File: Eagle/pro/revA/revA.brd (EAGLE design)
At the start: 100 x 88 mm, 57 parts, among them Q1 20MHz, U1 MCP42XXX

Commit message: silkscreen
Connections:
- net N$22 renamed LCD_GND
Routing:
- net N$28: track 106.1 -> 141.6 mm
- net N$21: track 132.2 -> 129.7 mm
- net N$29: track 94.9 -> 94.3 mm
- added copper zone on layer 1, net GND
- added copper zone on layer 16, net GND
- added copper zone on layer 1, net LCD_GND
- added copper zone on layer 16, net LCD_GND
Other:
- board size 100 x 88 mm -> 100 x 90 mm
- board text added: "Analyser"
- board text added: "Ashley J. Robinson"
- board text added: "Audio"
- board text added: "AudioSpectrumAnalyser"
- board text added: "DBG_UART"
- board text added: "GND"
- board text added: "IN"
- board text added: "OUT"
- board text added: "RESET"
- board text added: "RevA May 2014"
- board text added: "SW1"
- board text added: "SW2"
- board text added: "Spectrum"
- board text added: "TRIM"
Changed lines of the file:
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@@
 <setting verticaltext="up"/>
 </settings>
-<grid distance="0.5" unitdist="mm" unit="mm" style="lines" multiple="1" display="yes" altdistance="0.1" altunitdist="mm" altunit="mm"/>
+<grid distance="1" unitdist="mm" unit="mm" style="lines" multiple="1" display="yes" altdistance="0.1" altunitdist="mm" altunit="mm"/>
 <layers>
 <layer number="1" name="Top" color="4" fill="1" visible="yes" active="yes"/>
@@
 <board>
 <plain>
-<wire x1="0" y1="6" x2="0" y2="54" width="0" layer="20"/>
-<wire x1="6" y1="0" x2="94" y2="0" width="0" layer="20"/>
-<wire x1="100" y1="54" x2="100" y2="6" width="0" layer="20"/>
-<wire x1="6" y1="0" x2="0" y2="6" width="0" layer="20" curve="-90"/>
-<wire x1="100" y1="6" x2="94" y2="0" width="0" layer="20" curve="-90"/>
-<wire x1="0" y1="54" x2="6" y2="60" width="0" layer="20" curve="-90"/>
-<wire x1="8" y1="66" x2="8" y2="82" width="0" layer="20"/>
-<wire x1="14" y1="88" x2="87" y2="88" width="0" layer="20"/>
-<wire x1="92" y1="82" x2="92" y2="66" width="0" layer="20"/>
-<wire x1="92" y1="66" x2="86" y2="60" width="0" layer="20" curve="-90"/>
-<wire x1="87" y1="88" x2="92" y2="82" width="0" layer="20" curve="-90"/>
-<wire x1="8" y1="82" x2="14" y2="88" width="0" layer="20" curve="-90"/>
-<hole x="14.4" y="60" drill="0.5"/>
 <hole x="15.2" y="60" drill="0.5"/>
-<hole x="13.6" y="60" drill="0.5"/>
 <hole x="16.8" y="60" drill="0.5"/>
 <hole x="17.6" y="60" drill="0.5"/>
@@
 <hole x="84" y="60" drill="0.5"/>
 <hole x="82.4" y="60" drill="0.5"/>
+<hole x="84.8" y="60" drill="0.5"/>
+<hole x="12" y="60" drill="0.5"/>
+<hole x="13.6" y="60" drill="0.5"/>
+<hole x="14.4" y="60" drill="0.5"/>
+<hole x="12.8" y="60" drill="0.5"/>
+<hole x="4.8" y="60" drill="0.5"/>
+<hole x="6.4" y="60" drill="0.5"/>
+<hole x="7.2" y="60" drill="0.5"/>
+<hole x="5.6" y="60" drill="0.5"/>
+<hole x="8.8" y="60" drill="0.5"/>
+<hole x="9.6" y="60" drill="0.5"/>
+<hole x="8" y="60" drill="0.5"/>
+<hole x="11.2" y="60" drill="0.5"/>
+<hole x="10.4" y="60" drill="0.5"/>
+<hole x="1.6" y="60" drill="0.5"/>
+<hole x="3.2" y="60" drill="0.5"/>
+<hole x="4" y="60" drill="0.5"/>
+<hole x="2.4" y="60" drill="0.5"/>
+<hole x="0.8" y="60" drill="0.5"/>
 <hole x="85.6" y="60" drill="0.5"/>
 <hole x="86.4" y="60" drill="0.5"/>
-<hole x="84.8" y="60" drill="0.5"/>
-<wire x1="14" y1="60" x2="8" y2="66" width="0" layer="20" curve="-90"/>
-<wire x1="6" y1="60" x2="14" y2="60" width="0" layer="20"/>
-<wire x1="94" y1="60" x2="100" y2="54" width="0" layer="20" curve="-90"/>
-<wire x1="86" y1="60" x2="94" y2="60" width="0" layer="20"/>
+<hole x="88" y="60" drill="0.5"/>
+<hole x="88.8" y="60" drill="0.5"/>
+<hole x="87.2" y="60" drill="0.5"/>
+<hole x="90.4" y="60" drill="0.5"/>
+<hole x="91.2" y="60" drill="0.5"/>
+<hole x="89.6" y="60" drill="0.5"/>
+<hole x="92.8" y="60" drill="0.5"/>
+<hole x="93.6" y="60" drill="0.5"/>
+<hole x="92" y="60" drill="0.5"/>
+<hole x="95.2" y="60" drill="0.5"/>
+<hole x="96" y="60" drill="0.5"/>
+<hole x="94.4" y="60" drill="0.5"/>
+<hole x="97.6" y="60" drill="0.5"/>
+<hole x="98.4" y="60" drill="0.5"/>
+<hole x="96.8" y="60" drill="0.5"/>
+<hole x="99.2" y="60" drill="0.5"/>
+<wire x1="0" y1="6" x2="0" y2="84" width="0" layer="20"/>
+<wire x1="6" y1="90" x2="94" y2="90" width="0" layer="20"/>
+<wire x1="100" y1="84" x2="100" y2="6" width="0" layer="20"/>
+<wire x1="94" y1="0" x2="6" y2="0" width="0" layer="20"/>
+<wire x1="6" y1="0" x2="0" y2="6" width="0" layer="20" curve="-90"/>
+<wire x1="100" y1="6" x2="94" y2="0" width="0" layer="20" curve="-90"/>
+<wire x1="0" y1="84" x2="6" y2="90" width="0" layer="20" curve="-90"/>
+<wire x1="94" y1="90" x2="100" y2="84" width="0" layer="20" curve="-90"/>
+<text x="3" y="28" size="1.778" layer="21" font="vector">OUT</text>
+<text x="93" y="28" size="1.778" layer="21" font="vector">IN</text>
+<text x="3" y="11" size="1.778" layer="21" font="vector">OUT</text>
+<text x="93" y="11" size="1.778" layer="21" font="vector">IN</text>
+<text x="76" y="1" size="1.778" layer="21" font="vector">RESET</text>
+<text x="57" y="1" size="1.778" layer="21" font="vector">TRIM</text>
+<text x="38" y="1" size="1.778" layer="21" font="vector">SW2</text>
+<text x="18" y="1" size="1.778" layer="21" font="vector">SW1</text>
+<text x="27" y="52" size="1.778" layer="21" font="vector" rot="R270">GND</text>
+<text x="21" y="52" size="1.778" layer="21" font="vector" rot="R270">OUT</text>
+<text x="24" y="52" size="1.778" layer="21" font="vector" rot="R270">IN</text>
+<text x="20" y="43" size="1.778" layer="21" font="vector" rot="R90">DBG_UART</text>
+<text x="96" y="45" size="1.778" layer="22" font="vector" rot="MR0">Ashley J. Robinson</text>
+<text x="96" y="48" size="1.778" layer="22" font="vector" rot="MR0">AudioSpectrumAnalyser</text>
+<text x="96" y="42" size="1.778" layer="22" font="vector" rot="MR0">RevA May 2014</text>
+<text x="3" y="86" size="1.778" layer="21" font="vector">Audio</text>
+<text x="6" y="83" size="1.778" layer="21" font="vector">Spectrum</text>
+<text x="9" y="80" size="1.778" layer="21" font="vector">Analyser</text>
+<text x="1" y="76" size="1.778" layer="21" font="vector">Ashley J. Robinson</text>
+<text x="1" y="73" size="1.778" layer="21" font="vector">RevA May 2014</text>
 </plain>
 <attributes>
@@
 <wire x1="49.2508875" y1="38.2508875" x2="49.74709375" y2="38.74709375" width="0.254" layer="1"/>
 <wire x1="49.74709375" y1="38.74709375" x2="49.74709375" y2="42.0008875" width="0.254" layer="1"/>
+<polygon width="0.254" layer="16">
+<vertex x="-1" y="-1"/>
+<vertex x="-1" y="59"/>
+<vertex x="101" y="59"/>
+<vertex x="101" y="-1"/>
+</polygon>
+<polygon width="0.4064" layer="1">
+<vertex x="-1" y="-1"/>
+<vertex x="-1" y="59"/>
+<vertex x="101" y="59"/>
+<vertex x="101" y="-1"/>
+</polygon>
 </signal>
 <signal name="N$1">
@@
 <contactref element="SV2" pad="10"/>
 <contactref element="SV1" pad="1"/>
-<wire x1="9" y1="68.5" x2="26.5" y2="86" width="0.6096" layer="1"/>
-<wire x1="26.5" y1="86" x2="37.5" y2="86" width="0.6096" layer="1"/>
 <wire x1="37.5" y1="86" x2="37.5" y2="84" width="0.6096" layer="1"/>
 <wire x1="37.5" y1="84" x2="41.5" y2="80" width="0.6096" layer="1"/>
 <wire x1="41.5" y1="80" x2="72.5" y2="80" width="0.6096" layer="1"/>
-<wire x1="72.5" y1="80" x2="83.3" y2="69.2" width="0.6096" layer="1"/>
+<wire x1="72.5" y1="80" x2="79.5" y2="73" width="0.6096" layer="1"/>
+<wire x1="81.75" y1="70.75" x2="83.3" y2="69.2" width="0.6096" layer="1"/>
 <wire x1="83.3" y1="69.2" x2="83.3" y2="65.5" width="0.6096" layer="1"/>
 <wire x1="83.3" y1="65.5" x2="83.8" y2="65" width="0.6096" layer="1"/>
 <wire x1="83.8" y1="65" x2="85.81" y2="65" width="0.6096" layer="1"/>
 <wire x1="85.81" y1="65" x2="87.08" y2="66.27" width="0.6096" layer="1"/>
-<wire x1="12.92" y1="63.73" x2="9.77" y2="63.73" width="0.6096" layer="1"/>
-<wire x1="9.77" y1="63.73" x2="9" y2="64.5" width="0.6096" layer="1"/>
-<wire x1="9" y1="64.5" x2="9" y2="68.5" width="0.6096" layer="1"/>
+<wire x1="12.92" y1="63.73" x2="11.27" y2="63.73" width="0.6096" layer="1"/>
+<wire x1="11.27" y1="63.73" x2="9" y2="66" width="0.6096" layer="1"/>
+<wire x1="9" y1="66" x2="9" y2="68" width="0.6096" layer="1"/>
+<wire x1="9" y1="68" x2="14" y2="73" width="0.6096" layer="1"/>
+<wire x1="14" y1="73" x2="79.5" y2="73" width="0.6096" layer="1"/>
+<wire x1="79.5" y1="73" x2="81.75" y2="70.75" width="0.6096" layer="1"/>
 </signal>
 <signal name="N$29">
@@
 <wire x1="39" y1="84" x2="39" y2="86" width="0.6096" layer="16"/>
 <wire x1="39" y1="86" x2="39" y2="84.5" width="0.6096" layer="1"/>
-<wire x1="39" y1="84.5" x2="42" y2="81.5" width="0.6096" layer="1"/>
-<wire x1="42" y1="81.5" x2="73.5" y2="81.5" width="0.6096" layer="1"/>
-<wire x1="73.5" y1="81.5" x2="84.54" y2="70.46" width="0.6096" layer="1"/>
-<wire x1="84.54" y1="70.46" x2="84.54" y2="66.27" width="0.6096" layer="1"/>
+<wire x1="84.54" y1="66.27" x2="84.54" y2="69.46" width="0.6096" layer="1"/>
+<wire x1="84.54" y1="69.46" x2="73" y2="81" width="0.6096" layer="1"/>
+<wire x1="73" y1="81" x2="42.5" y2="81" width="0.6096" layer="1"/>
+<wire x1="39" y1="84.5" x2="42.5" y2="81" width="0.6096" layer="1"/>
 </signal>
 <signal name="N$30">
@@
 <wire x1="31.04" y1="63.73" x2="28.5" y2="66.27" width="0.6096" layer="1"/>
 <wire x1="45" y1="86" x2="45" y2="84.5" width="0.6096" layer="1"/>
-<wire x1="45" y1="84.5" x2="46.5" y2="83" width="0.6096" layer="1"/>
-<wire x1="71.5" y1="86" x2="89.5" y2="68" width="0.6096" layer="1"/>
+<wire x1="45" y1="84.5" x2="47.5" y2="82" width="0.6096" layer="1"/>
 <wire x1="79.46" y1="63.96" x2="79.46" y2="63.73" width="0.6096" layer="1"/>
 <wire x1="79.46" y1="63.96" x2="81.92" y2="61.5" width="0.6096" layer="1"/>
@@
 <wire x1="87.5" y1="61.5" x2="89.5" y2="63.5" width="0.6096" layer="1"/>
 <wire x1="89.5" y1="63.5" x2="89.5" y2="68" width="0.6096" layer="1"/>
-<wire x1="71.5" y1="86" x2="66.5" y2="86" width="0.6096" layer="1"/>
-<wire x1="66.5" y1="86" x2="63.5" y2="83" width="0.6096" layer="1"/>
-<wire x1="63.5" y1="83" x2="46.5" y2="83" width="0.6096" layer="1"/>
-</signal>
-<signal name="N$22">
+<wire x1="89.5" y1="68" x2="75.5" y2="82" width="0.6096" layer="1"/>
+<wire x1="75.5" y1="82" x2="47.5" y2="82" width="0.6096" layer="1"/>
+</signal>
+<signal name="LCD_GND">
 <contactref element="SV1" pad="6"/>
 <contactref element="SV2" pad="5"/>
@@
 <wire x1="12.92" y1="66.27" x2="15.46" y2="66.27" width="0.6096" layer="1"/>
 <wire x1="15.46" y1="66.27" x2="18" y2="66.27" width="0.6096" layer="1"/>
+<polygon width="0.4064" layer="16">
+<vertex x="-1" y="61"/>
+<vertex x="-1" y="91"/>
+<vertex x="101" y="91"/>
+<vertex x="101" y="61"/>
+</polygon>
+<polygon width="0.4064" layer="1">
+<vertex x="-1" y="61"/>
+<vertex x="-1" y="91"/>
+<vertex x="101" y="91"/>
+<vertex x="101" y="61"/>
+</polygon>
 </signal>
 <signal name="LCD_RST">

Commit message: track opt
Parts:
- moved R1 3.50 mm to (75.5, 46.0)
- moved R2 3.50 mm to (72.0, 46.0)
- moved R12 2.55 mm to (19.5, 25.0), turned to 270 degrees
- moved R10 2.00 mm to (49.0, 51.0)
- moved R11 2.00 mm to (51.5, 51.0)
- turned C3 to 270 degrees
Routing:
- net TCK: track 82.5 -> 63.6 mm
- net DIG_POT_RST: track 34.5 -> 47.7 mm, vias 4 -> 2
- net VCC: track 257.3 -> 268.9 mm, vias 3 -> 4
- net DIGI_RES_RIGHT: track 89.0 -> 77.7 mm
- net N$20: track 50.0 -> 61.3 mm, vias 3 -> 1
- net TMS: track 68.8 -> 73.2 mm, vias 4 -> 3
- net GND: track 455.2 -> 458.8 mm, vias 7 -> 4
- net N$11: track 23.9 -> 21.1 mm
- net SCLK: track 105.8 -> 103.2 mm, vias 3 -> 4
- net N$3: track 5.91 -> 3.30 mm
- net MOSI: track 81.4 -> 83.8 mm, vias 4 -> 3
- net N$14: track 39.8 -> 37.6 mm
- net USB_D-: track 5.91 -> 7.91 mm
- net USB_D+: track 6.12 -> 8.12 mm
- net N$4: track 5.36 -> 3.36 mm
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
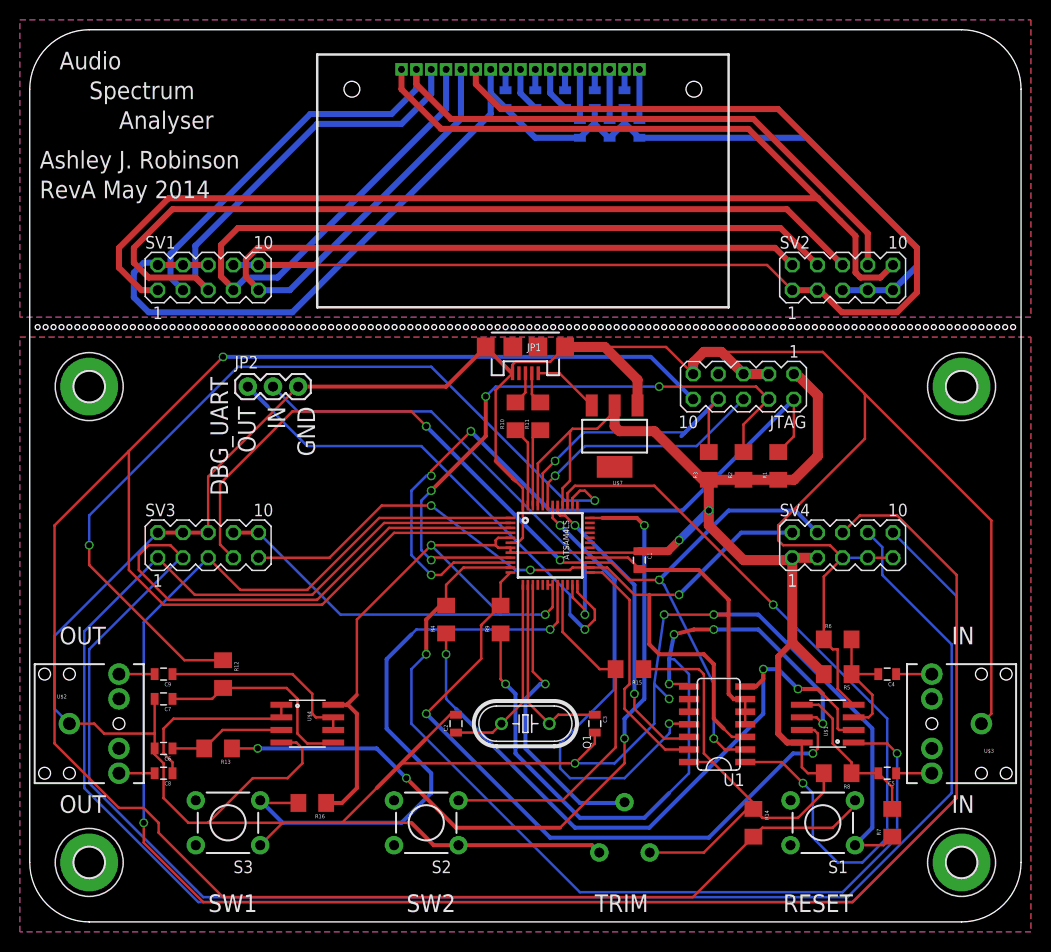
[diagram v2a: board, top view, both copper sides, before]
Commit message: tracking thickening and silkscreen tidy
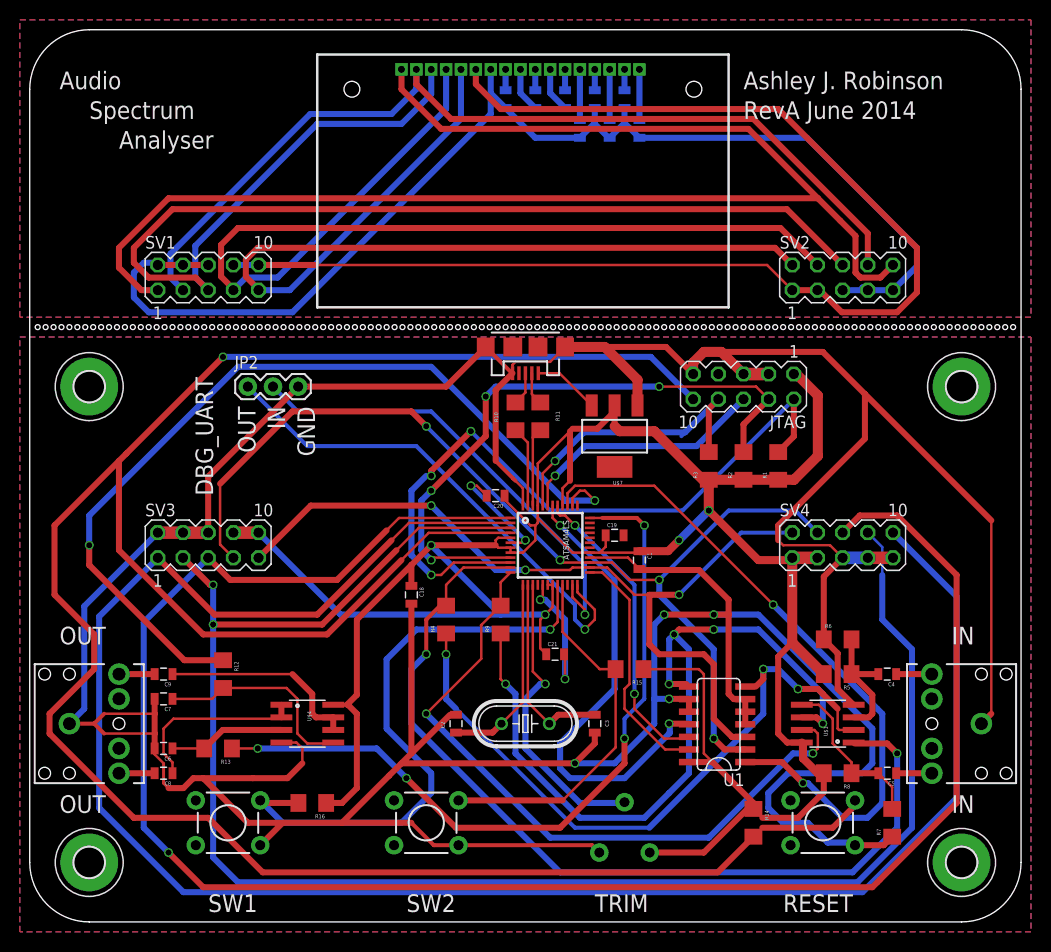
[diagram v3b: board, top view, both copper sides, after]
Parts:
- added C18, C19, C20, C21: 100nF, SparkFun:0805
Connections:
- net GND: now also C18.2, C19.2, C20.2, C21.2
- net VCC: now also C18.1, C19.1, C20.1, C21.1
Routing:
- net GND: track 458.8 -> 516.9 mm, vias 4 -> 8
- net LCD_RST: track 201.3 -> 171.4 mm, vias 0 -> 2
- net VCC: track 268.9 -> 285.9 mm
- net DIG_POT_CS: track 77.7 -> 68.6 mm
- net LCD_AD: track 192.3 -> 189.6 mm
- net DIGI_RES_RIGHT: track 77.7 -> 80.0 mm
- net AUDIO_LEFT: track 94.9 -> 92.7 mm
- net NRESET: track 242.3 -> 244.4 mm
- net SCLK: track 103.2 -> 104.1 mm
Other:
- board text added: "RevA June 2014"
- board text removed: "RevA May 2014"
